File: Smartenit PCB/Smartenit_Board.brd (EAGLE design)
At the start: 55.3 x 72.5 mm, 85 parts, among them J3 2X5CONNECTOR1.27MM, Q1 QUARTZ_3.58M_2PIN, U1 ADE7953, U2 ESP-WROOM-32, U3 SN74LVC1G3157

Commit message: new no error
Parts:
- moved J2 0.40 mm to (2.18, -68.2)
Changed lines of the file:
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@@
 <attribute name="PROD_ID" value="CONN-08438" x="3.13" y="-56.38" size="1.778" layer="27" display="off"/>
 </element>
-<element name="J2" library="SparkFun-Connectors" package="1X06" value="" x="1.8" y="-68.37">
-<attribute name="PROD_ID" value="CONN-08437" x="1.8" y="-68.37" size="1.778" layer="27" display="off"/>
+<element name="J2" library="SparkFun-Connectors" package="1X06" value="" x="2.18" y="-68.24">
+<attribute name="PROD_ID" value="CONN-08437" x="2.18" y="-68.24" size="1.778" layer="27" display="off"/>
 </element>
 <element name="U$1" library="Smart_Charger" package="SOIC8" value="MP1584" x="33.32" y="-57.07" rot="R90"/>
@@
 <contactref element="C25" pad="2"/>
 <contactref element="R36" pad="1"/>
-<wire x1="5.67" y1="-56.38" x2="4.34" y2="-68.37" width="0" layer="19" extent="1-1"/>
+<wire x1="5.67" y1="-56.38" x2="4.72" y2="-68.24" width="0" layer="19" extent="1-1"/>
 <wire x1="18.98" y1="-46.55" x2="5.67" y2="-56.38" width="0" layer="19" extent="1-1"/>
 <wire x1="17.76" y1="-43.52" x2="18.98" y2="-46.55" width="0" layer="19" extent="1-1"/>
@@
 <contactref element="U$3" pad="4"/>
 <contactref element="R27" pad="1"/>
-<wire x1="32.5" y1="-65.63" x2="1.8" y2="-68.37" width="0" layer="19" extent="1-1"/>
+<wire x1="32.5" y1="-65.63" x2="2.18" y2="-68.24" width="0" layer="19" extent="1-1"/>
 <wire x1="30.72" y1="-57.705" x2="32.5" y2="-65.63" width="0" layer="19" extent="1-1"/>
 <wire x1="38.5" y1="-54.73" x2="30.72" y2="-57.705" width="0" layer="19" extent="1-1"/>
@@
 <contactref element="J2" pad="6"/>
 <contactref element="R20" pad="2"/>
-<wire x1="25.87" y1="-68.87" x2="14.5" y2="-68.37" width="0" layer="19" extent="1-1"/>
+<wire x1="25.87" y1="-68.87" x2="14.88" y2="-68.24" width="0" layer="19" extent="1-1"/>
 </signal>
 <signal name="-12V">
@@
 <contactref element="R29" pad="1"/>
 <contactref element="C22" pad="2"/>
-<wire x1="3.8" y1="-19.49" x2="6.88" y2="-68.37" width="0" layer="19" extent="1-1"/>
+<wire x1="3.8" y1="-19.49" x2="7.26" y2="-68.24" width="0" layer="19" extent="1-1"/>
 <wire x1="8.65" y1="-17.56" x2="3.8" y2="-19.49" width="0" layer="19" extent="1-1"/>
 <wire x1="29.46" y1="-3.31" x2="8.65" y2="-17.56" width="0" layer="19" extent="1-1"/>

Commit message: no error still
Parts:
- moved J1 0.13 mm to (3.13, -56.5)
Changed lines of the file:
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@@
 <element name="C4" library="Nizanlib" package="0402-CAP" value="104n" x="8.35" y="-34.61"/>
 <element name="C9" library="SparkFun" package="CPOL-RADIAL-10UF-25V" value="" x="25.92" y="-63.2"/>
-<element name="J1" library="SparkFun-Connectors" package="1X08" value="" x="3.13" y="-56.38">
-<attribute name="PROD_ID" value="CONN-08438" x="3.13" y="-56.38" size="1.778" layer="27" display="off"/>
+<element name="J1" library="SparkFun-Connectors" package="1X08" value="" x="3.13" y="-56.51">
+<attribute name="PROD_ID" value="CONN-08438" x="3.13" y="-56.51" size="1.778" layer="27" display="off"/>
 </element>
 <element name="J2" library="SparkFun-Connectors" package="1X06" value="" x="2.18" y="-68.24">
@@
 <contactref element="R12" pad="1"/>
 <contactref element="J1" pad="6"/>
-<wire x1="9.41" y1="-39.75" x2="15.83" y2="-56.38" width="0" layer="19" extent="1-1"/>
+<wire x1="9.41" y1="-39.75" x2="15.83" y2="-56.51" width="0" layer="19" extent="1-1"/>
 <wire x1="7.78" y1="-32.3" x2="9.41" y2="-39.75" width="0" layer="19" extent="1-1"/>
 </signal>
@@
 <contactref element="R7" pad="1"/>
 <contactref element="J1" pad="5"/>
-<wire x1="5.35" y1="-39.76" x2="13.29" y2="-56.38" width="0" layer="19" extent="1-1"/>
+<wire x1="5.35" y1="-39.76" x2="13.29" y2="-56.51" width="0" layer="19" extent="1-1"/>
 <wire x1="4.64" y1="-32.3" x2="5.35" y2="-39.76" width="0" layer="19" extent="1-1"/>
 </signal>
@@
 <contactref element="C25" pad="2"/>
 <contactref element="R36" pad="1"/>
-<wire x1="5.67" y1="-56.38" x2="4.72" y2="-68.24" width="0" layer="19" extent="1-1"/>
-<wire x1="18.98" y1="-46.55" x2="5.67" y2="-56.38" width="0" layer="19" extent="1-1"/>
+<wire x1="5.67" y1="-56.51" x2="4.72" y2="-68.24" width="0" layer="19" extent="1-1"/>
+<wire x1="18.98" y1="-46.55" x2="5.67" y2="-56.51" width="0" layer="19" extent="1-1"/>
 <wire x1="17.76" y1="-43.52" x2="18.98" y2="-46.55" width="0" layer="19" extent="1-1"/>
 <wire x1="17.761" y1="-42.344" x2="17.76" y2="-43.52" width="0" layer="19" extent="1-1"/>
@@
 <contactref element="R4" pad="1"/>
 <contactref element="J1" pad="8"/>
-<wire x1="16.66" y1="-43.52" x2="20.91" y2="-56.38" width="0" layer="19" extent="1-1"/>
+<wire x1="16.66" y1="-43.52" x2="20.91" y2="-56.51" width="0" layer="19" extent="1-1"/>
 <wire x1="16.64" y1="-42.33" x2="16.66" y2="-43.52" width="0" layer="19" extent="1-1"/>
 </signal>
@@
 <contactref element="R22" pad="1"/>
 <contactref element="J1" pad="7"/>
-<wire x1="18.98" y1="-45.45" x2="18.37" y2="-56.38" width="0" layer="19" extent="1-1"/>
+<wire x1="18.98" y1="-45.45" x2="18.37" y2="-56.51" width="0" layer="19" extent="1-1"/>
 <wire x1="18.93" y1="-42.37" x2="18.98" y2="-45.45" width="0" layer="19" extent="1-1"/>
 </signal>
@@
 <contactref element="R32" pad="2"/>
 <contactref element="D6" pad="C"/>
-<wire x1="2.93" y1="-17.52" x2="3.13" y2="-56.38" width="0" layer="19" extent="1-1"/>
+<wire x1="2.93" y1="-17.52" x2="3.13" y2="-56.51" width="0" layer="19" extent="1-1"/>
 <wire x1="19.31" y1="-6.75" x2="2.93" y2="-17.52" width="0" layer="19" extent="1-1"/>
 <wire x1="22.26" y1="-5.85" x2="19.31" y2="-6.75" width="0" layer="19" extent="1-1"/>
@@
 <contactref element="J1" pad="3"/>
 <contactref element="R34" pad="1"/>
-<wire x1="25.83" y1="-20.18" x2="8.21" y2="-56.38" width="0" layer="19" extent="1-1"/>
+<wire x1="25.83" y1="-20.18" x2="8.21" y2="-56.51" width="0" layer="19" extent="1-1"/>
 </signal>
 <signal name="LNV1">
 <contactref element="J1" pad="4"/>
 <contactref element="R35" pad="1"/>
-<wire x1="28.52" y1="-19.2" x2="10.75" y2="-56.38" width="0" layer="19" extent="1-1"/>
+<wire x1="28.52" y1="-19.2" x2="10.75" y2="-56.51" width="0" layer="19" extent="1-1"/>
 </signal>
 <signal name="DIO12">

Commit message: no error
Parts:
- moved J1 0.13 mm to (3.13, -56.6)
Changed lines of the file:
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@@
 <element name="C4" library="Nizanlib" package="0402-CAP" value="104n" x="8.35" y="-34.61"/>
 <element name="C9" library="SparkFun" package="CPOL-RADIAL-10UF-25V" value="" x="25.92" y="-63.2"/>
-<element name="J1" library="SparkFun-Connectors" package="1X08" value="" x="3.13" y="-56.51">
-<attribute name="PROD_ID" value="CONN-08438" x="3.13" y="-56.51" size="1.778" layer="27" display="off"/>
+<element name="J1" library="SparkFun-Connectors" package="1X08" value="" x="3.13" y="-56.64">
+<attribute name="PROD_ID" value="CONN-08438" x="3.13" y="-56.64" size="1.778" layer="27" display="off"/>
 </element>
 <element name="J2" library="SparkFun-Connectors" package="1X06" value="" x="2.18" y="-68.24">
@@
 <contactref element="R12" pad="1"/>
 <contactref element="J1" pad="6"/>
-<wire x1="9.41" y1="-39.75" x2="15.83" y2="-56.51" width="0" layer="19" extent="1-1"/>
+<wire x1="9.41" y1="-39.75" x2="15.83" y2="-56.64" width="0" layer="19" extent="1-1"/>
 <wire x1="7.78" y1="-32.3" x2="9.41" y2="-39.75" width="0" layer="19" extent="1-1"/>
 </signal>
@@
 <contactref element="R7" pad="1"/>
 <contactref element="J1" pad="5"/>
-<wire x1="5.35" y1="-39.76" x2="13.29" y2="-56.51" width="0" layer="19" extent="1-1"/>
+<wire x1="5.35" y1="-39.76" x2="13.29" y2="-56.64" width="0" layer="19" extent="1-1"/>
 <wire x1="4.64" y1="-32.3" x2="5.35" y2="-39.76" width="0" layer="19" extent="1-1"/>
 </signal>
@@
 <contactref element="C25" pad="2"/>
 <contactref element="R36" pad="1"/>
-<wire x1="5.67" y1="-56.51" x2="4.72" y2="-68.24" width="0" layer="19" extent="1-1"/>
-<wire x1="18.98" y1="-46.55" x2="5.67" y2="-56.51" width="0" layer="19" extent="1-1"/>
+<wire x1="5.67" y1="-56.64" x2="4.72" y2="-68.24" width="0" layer="19" extent="1-1"/>
+<wire x1="18.98" y1="-46.55" x2="5.67" y2="-56.64" width="0" layer="19" extent="1-1"/>
 <wire x1="17.76" y1="-43.52" x2="18.98" y2="-46.55" width="0" layer="19" extent="1-1"/>
 <wire x1="17.761" y1="-42.344" x2="17.76" y2="-43.52" width="0" layer="19" extent="1-1"/>
@@
 <contactref element="R4" pad="1"/>
 <contactref element="J1" pad="8"/>
-<wire x1="16.66" y1="-43.52" x2="20.91" y2="-56.51" width="0" layer="19" extent="1-1"/>
+<wire x1="16.66" y1="-43.52" x2="20.91" y2="-56.64" width="0" layer="19" extent="1-1"/>
 <wire x1="16.64" y1="-42.33" x2="16.66" y2="-43.52" width="0" layer="19" extent="1-1"/>
 </signal>
@@
 <contactref element="R22" pad="1"/>
 <contactref element="J1" pad="7"/>
-<wire x1="18.98" y1="-45.45" x2="18.37" y2="-56.51" width="0" layer="19" extent="1-1"/>
+<wire x1="18.98" y1="-45.45" x2="18.37" y2="-56.64" width="0" layer="19" extent="1-1"/>
 <wire x1="18.93" y1="-42.37" x2="18.98" y2="-45.45" width="0" layer="19" extent="1-1"/>
 </signal>
@@
 <contactref element="R32" pad="2"/>
 <contactref element="D6" pad="C"/>
-<wire x1="2.93" y1="-17.52" x2="3.13" y2="-56.51" width="0" layer="19" extent="1-1"/>
+<wire x1="2.93" y1="-17.52" x2="3.13" y2="-56.64" width="0" layer="19" extent="1-1"/>
 <wire x1="19.31" y1="-6.75" x2="2.93" y2="-17.52" width="0" layer="19" extent="1-1"/>
 <wire x1="22.26" y1="-5.85" x2="19.31" y2="-6.75" width="0" layer="19" extent="1-1"/>
@@
 <contactref element="J1" pad="3"/>
 <contactref element="R34" pad="1"/>
-<wire x1="25.83" y1="-20.18" x2="8.21" y2="-56.51" width="0" layer="19" extent="1-1"/>
+<wire x1="25.83" y1="-20.18" x2="8.21" y2="-56.64" width="0" layer="19" extent="1-1"/>
 </signal>
 <signal name="LNV1">
 <contactref element="J1" pad="4"/>
 <contactref element="R35" pad="1"/>
-<wire x1="28.52" y1="-19.2" x2="10.75" y2="-56.51" width="0" layer="19" extent="1-1"/>
+<wire x1="28.52" y1="-19.2" x2="10.75" y2="-56.64" width="0" layer="19" extent="1-1"/>
 </signal>
 <signal name="DIO12">

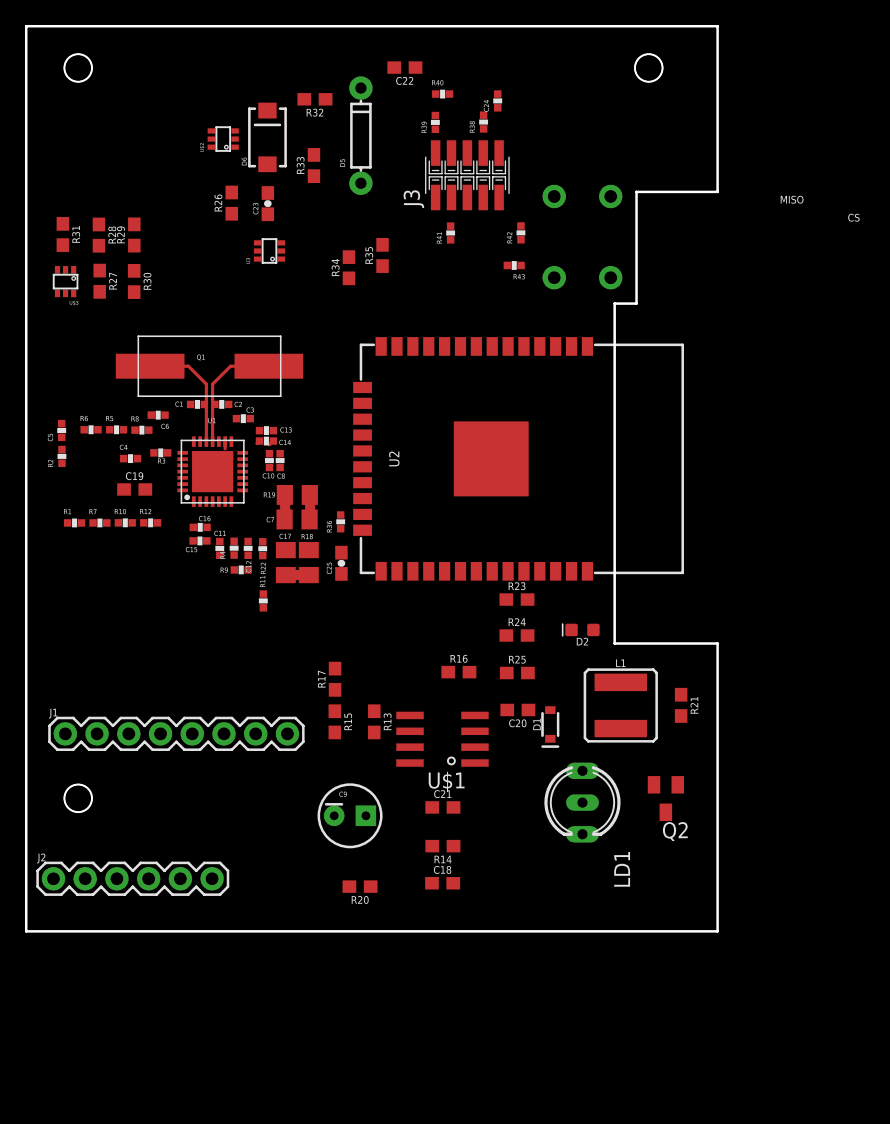
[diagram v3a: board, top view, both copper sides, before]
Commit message: update (google drive supported now)
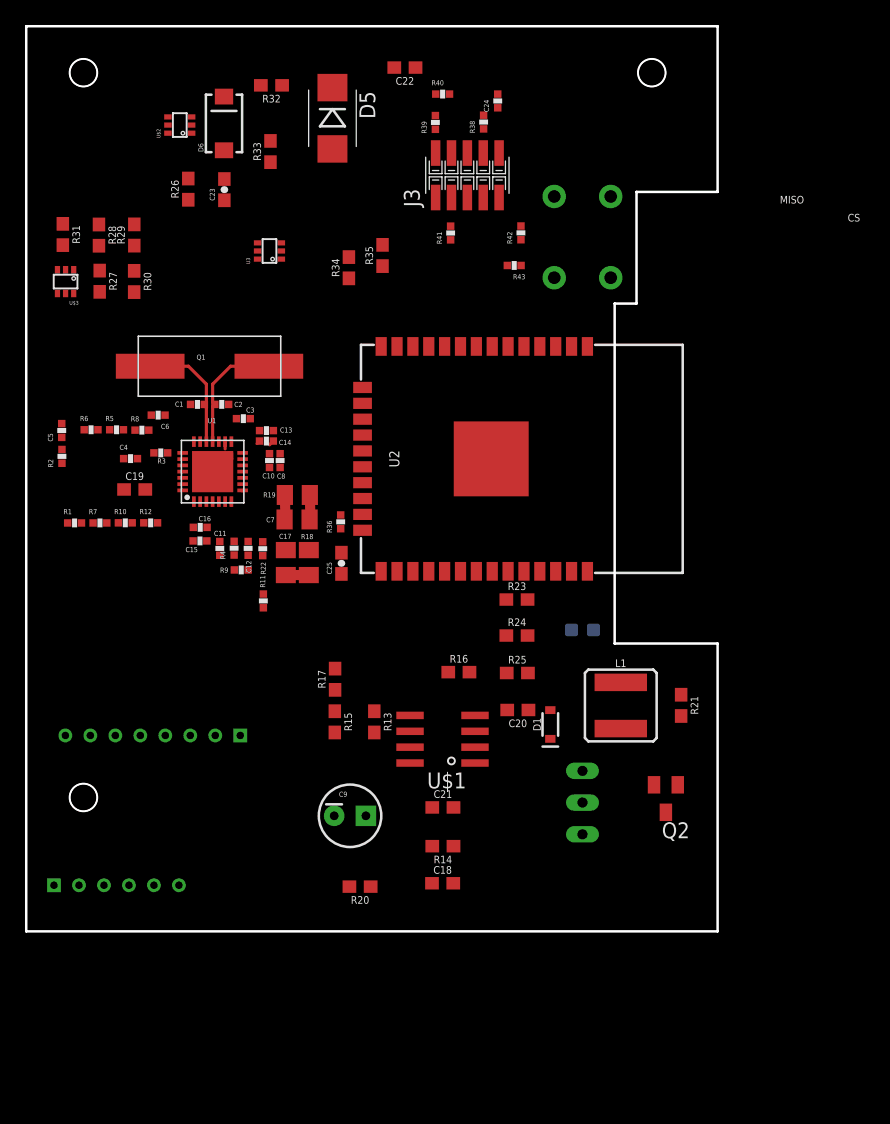
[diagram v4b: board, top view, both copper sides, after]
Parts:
- removed J1: (no value), SparkFun-Connectors:1X08
- removed J2: (no value), SparkFun-Connectors:1X06
- added U$4: 2MM_CONN8, Smart_Charger:CONN82MM
- added U$5: 2MM_CONN6, Smart_Charger:CONN6_2MM
- D5: device SparkFun:DIODE-1N4148 -> SparkFun:DIODE-HV
- moved R33 3.66 mm to (19.6, -10.0)
- moved C23 3.66 mm to (15.9, -13.1)
- moved R32 3.66 mm to (19.6, -4.73)
- moved D6 3.66 mm to (15.8, -7.78)
- moved R26 3.66 mm to (13.0, -13.0)
- moved U$2 3.66 mm to (13.2, -8.56)
- moved D5 2.67 mm to (24.5, -7.37), turned to 270 degrees
- flipped D2 to the bottom
- flipped LD1 to the bottom
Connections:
- net -12V: now also U$5.4; no longer J2.3
- net 12V: now also U$5.6; no longer J2.1
- net DIO11: now also U$5.2; no longer J2.5
- net DIO12: now also U$5.3; no longer J2.4
- net GND: now also U$4.7, U$5.5; no longer J1.2, J2.2
- net IAN: now also U$4.2; no longer J1.7
- net IAP: now also U$4.1; no longer J1.8
- net IBN: now also U$4.4; no longer J1.5
- net IBP: now also U$4.3; no longer J1.6
- net LNV1: now also U$4.5; no longer J1.4
- net LNV2: now also U$4.6; no longer J1.3
- net N$38: now also U$5.1; no longer J2.6
- net PILOT: now also U$4.8; no longer J1.1
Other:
- outline, holes or cut-outs redrawn

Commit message: routed board
routed and added pin connections to ESp module
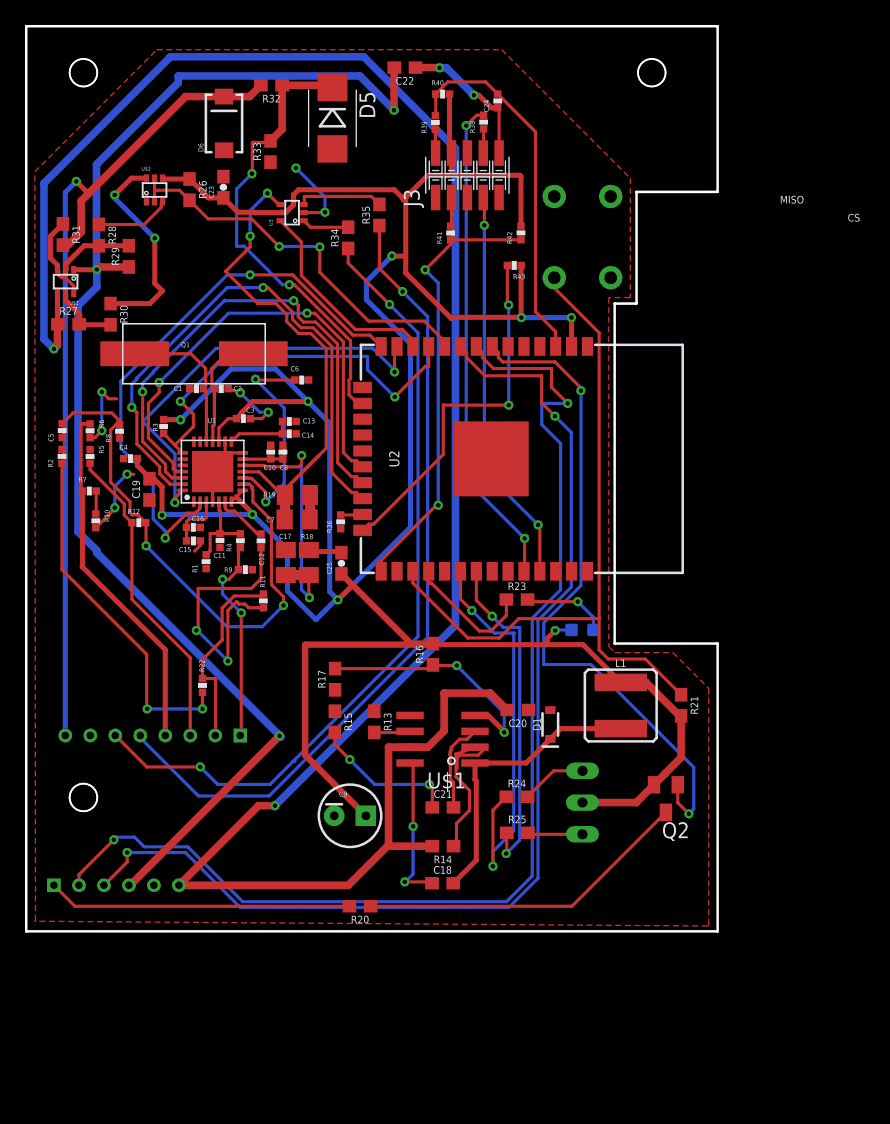
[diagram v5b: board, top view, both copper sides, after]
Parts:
- moved R24 12.9 mm to (39.3, -61.7)
- moved R25 12.8 mm to (39.3, -64.6)
- moved R22 12.0 mm to (14.1, -52.8), turned to 270 degrees
- moved C6 11.8 mm to (22.1, -28.3), turned to 0 degrees
- moved R1 11.0 mm to (14.4, -42.9), turned to 90 degrees
- moved U$2 6.58 mm to (9.62, -14.1), turned to 0 degrees
- moved R27 4.25 mm to (3.39, -23.9), turned to 0 degrees
- moved U3 3.56 mm to (22.2, -15.6)
- moved R35 3.25 mm to (28.3, -15.1)
- moved R30 3.23 mm to (6.75, -23.1)
- moved R5 3.01 mm to (5.11, -34.4), turned to 270 degrees
- moved R7 2.70 mm to (5.05, -37.2)
- moved R16 2.52 mm to (32.5, -50.3), turned to 90 degrees
- moved R34 2.39 mm to (25.8, -16.9)
- moved R10 2.37 mm to (5.57, -39.6), turned to 270 degrees
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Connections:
- removed net MISO: U2.21
- removed net MOSI: U2.22
- removed net N$34: U2.14
- removed net N$35: U2.13
- removed net N$36: U2.12
- removed net N$37: U2.11
- removed net N$41: U2.10
- removed net N$42: U2.9
- removed net N$43: U2.8
- removed net N$44: U2.7
- removed net N$48: U2.30
- removed net N$49: U2.31
- removed net N$50: U2.28
- removed net N$51: U2.27
- removed net N$52: U2.26
- removed net SPICLK: U2.20
- removed net VCC: R3.1
- net 3.3V: now also R3.1
- net ADC1: now also U2.16
- net DIO0: now also U2.13
- net DIO1: now also U2.12
- net DIO10: now also U2.7
- net DIO11: now also U2.8
- net DIO12: now also U2.9
- net DIO13: now also U2.10
- net DIO16: now also U2.30
- net DIO17: now also U2.31
- net DIO5: now also U2.11
- net DIO8: now also U2.27
- net DIO9: now also U2.28
- net RESET_ISO: now also U2.14
- net SPIMISO: now also U2.21
- net SPIMOSI: now also U2.22
- net SPISCLK: now also U2.20
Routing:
- net 3.3V: track 0.33 -> 248.6 mm, vias 0 -> 9
- net 12V: track 0.00 -> 170.4 mm, vias 0 -> 2
- net -12V: track 0.00 -> 106.8 mm, vias 0 -> 3
- net DIO11: track 0.00 -> 93.1 mm, vias 0 -> 2
- net DIO12: track 0.00 -> 89.1 mm, vias 0 -> 2
- net PILOT: track 0.00 -> 68.7 mm, vias 0 -> 1
- net GND: track 6.56 -> 72.7 mm, vias 0 -> 12
- net LNV1: track 0.00 -> 64.9 mm, vias 0 -> 1
- net LNV2: track 0.00 -> 64.3 mm, vias 0 -> 2
- net DIO8: track 0.00 -> 57.6 mm
- net DIO10: track 0.00 -> 54.1 mm, vias 0 -> 2
- net SPIMOSI: track 0.00 -> 45.3 mm, vias 0 -> 2
- net RESET_ISO: track 0.00 -> 45.2 mm, vias 0 -> 2
- net N$5: track 0.00 -> 42.9 mm, vias 0 -> 2
- net SPIMISO: track 0.00 -> 42.0 mm, vias 0 -> 2
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- added copper zone on layer 1, net GND
